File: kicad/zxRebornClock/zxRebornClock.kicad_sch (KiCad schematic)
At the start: 107 parts, among them J1 Jack DC, J2 USB_B_Micro, J3 Conn_01x04, J4 Conn_01x03, J5 Conn_01x03, J6 Conn_01x02, Q1 MMBTA42, Q10 MMBTA42, Q2 MMBTA42, Q3 MMBTA42, Q4 MMBTA42, Q5 MMBTA42, Q6 MMBTA42, Q7 MMBTA42, Q8 MMBTA42, Q9 MMBTA42, SW1 RESET, SW2 D, SW3 HH, SW4 MM, SW5 SS, SW6 F, U1 CH32X035C8T6, U10 TLP627, U2 AMS1117-3.3, U3 12V->200V, U4 USBLC6-4SC6, U5 DS1302, U6 ESP-12F, U7 TLP627, U8 TLP627, U9 TLP627, Y1 32768

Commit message: work in progress
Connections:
- net B_F: now also U1.41 (PA9); no longer U1.24 (PB4)
- net B_HH: now also U1.38 (PC14)
- net B_MM: now also U1.39 (PC15)
- net B_SS: now also U1.40 (PA8); no longer U1.23 (PB3)
- no-connect marks 27 -> 25
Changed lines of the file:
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@@
-	)
-	(no_connect
-		(at 46.99 139.7)
 	)
 	(no_connect
@@
 	)
 	(no_connect
+		(at 57.15 185.42)
+	)
+	(no_connect
 		(at 138.43 232.41)
-	)
-	(no_connect
-		(at 52.07 139.7)
 	)
 	(no_connect
@@
 	)
 	(no_connect
-		(at 49.53 139.7)
-	)
-	(no_connect
 		(at 138.43 224.79)
 	)
@@
 	)
 	(no_connect
-		(at 54.61 139.7)
-	)
-	(no_connect
 		(at 168.91 222.25)
 	)
@@
 	(no_connect
 		(at 20.32 156.21)
+	)
+	(no_connect
+		(at 54.61 185.42)
 	)
 	(no_connect
@@
 	)
 	(label "B_MM"
-		(at 1.905 186.69 0)
+		(at 52.07 139.7 90)
 		(effects
 			(font
@@
 	)
 	(label "B_F"
-		(at 57.15 185.42 270)
-		(effects
-			(font
-				(size 1.27 1.27)
-			)
-			(justify right bottom)
+		(at 46.99 139.7 90)
+		(effects
+			(font
+				(size 1.27 1.27)
+			)
+			(justify left bottom)
 		)
 	)
@@
 	)
 	(label "B_HH"
-		(at 1.905 191.135 0)
+		(at 54.61 139.7 90)
 		(effects
 			(font
@@
 	)
 	(label "B_SS"
-		(at 54.61 185.42 270)
-		(effects
-			(font
-				(size 1.27 1.27)
-			)
-			(justify right bottom)
-		)
-	)
+		(at 49.53 139.7 90)
+		(effects
+			(font
+				(size 1.27 1.27)
+			)
+			(justify left bottom)
+		)
+	)

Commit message: work in progress
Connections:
- net DOWNLOAD: now also U4.3 (I/O2), U4.4 (I/O3); no longer U4.1 (I/O1), U4.6 (I/O4)
- net UDM: now also U4.1 (I/O1), U4.6 (I/O4); no longer U4.3 (I/O2), U4.4 (I/O3)
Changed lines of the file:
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@@
 	)
 	(label "UDP"
-		(at 50.8 204.47 180)
+		(at 50.8 207.01 180)
 		(effects
 			(font
@@
 	)
 	(label "UDM"
-		(at 50.8 207.01 180)
+		(at 50.8 204.47 180)
 		(effects
 			(font
@@
 	)
 	(label "UDM"
-		(at 50.8 209.55 180)
+		(at 50.8 212.09 180)
 		(effects
 			(font
@@
 	)
 	(label "UDP"
-		(at 50.8 212.09 180)
-		(effects
-			(font
+		(at 50.8 209.55 180)
+		(effects
+			(font

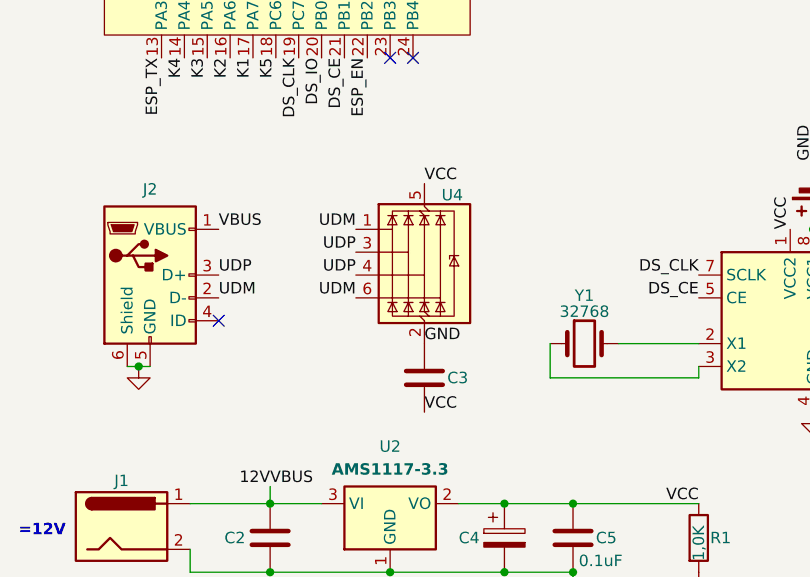
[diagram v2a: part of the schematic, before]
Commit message: fix schema
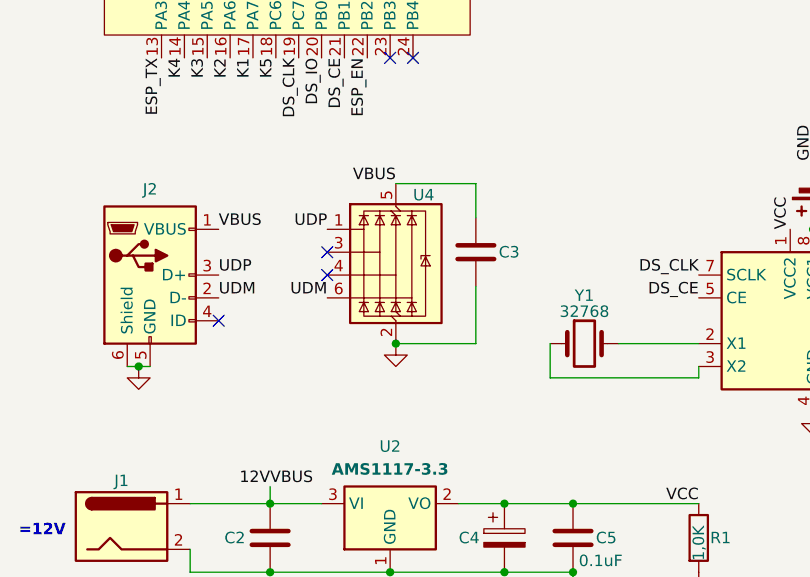
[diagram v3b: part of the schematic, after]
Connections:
- net 12V: now also C3.1, U4.5 (VBUS)
- net DOWNLOAD: now also U4.1 (I/O1); no longer U4.3 (I/O2), U4.4 (I/O3)
- net GND: now also C3.2; no longer C3.1
- net UDM: no longer U4.1 (I/O1)
- net VCC: no longer C3.2, U4.5 (VBUS)
- no-connect marks 25 -> 27
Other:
- moved on the sheet: C3, U4
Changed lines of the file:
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@@
 	)
 	(junction
+		(at 55.245 217.17)
+		(diameter 0)
+		(color 0 0 0 0)
+	)
+	(junction
 		(at 74.93 234.95)
 		(diameter 0)
@@
 	)
 	(no_connect
+		(at 47.625 207.01)
+	)
+	(no_connect
 		(at 138.43 229.87)
 	)
@@
 	)
 	(no_connect
+		(at 47.625 209.55)
+	)
+	(no_connect
 		(at 138.43 219.71)
 	)
@@
 	(wire
 		(pts
+			(xy 55.245 199.39) (xy 64.135 199.39)
+		)
+		(stroke
+			(width 0)
+			(type default)
+		)
+	)
+	(wire
+		(pts
 			(xy 170.18 124.46) (xy 175.26 124.46)
 		)
@@
 	(wire
 		(pts
+			(xy 64.135 210.82) (xy 64.135 217.17)
+		)
+		(stroke
+			(width 0)
+			(type default)
+		)
+	)
+	(wire
+		(pts
 			(xy 184.15 53.975) (xy 184.15 48.895)
 		)
@@
 	(wire
 		(pts
+			(xy 64.135 199.39) (xy 64.135 203.2)
+		)
+		(stroke
+			(width 0)
+			(type default)
+		)
+	)
+	(wire
+		(pts
 			(xy 29.21 137.16) (xy 24.13 137.16)
 		)
@@
 	(wire
 		(pts
+			(xy 64.135 217.17) (xy 55.245 217.17)
+		)
+		(stroke
+			(width 0)
+			(type default)
+		)
+	)
+	(wire
+		(pts
 			(xy 74.93 242.57) (xy 74.93 250.19)
 		)
@@
 		)
 	)
+	(label "VBUS"
+		(at 55.245 199.39 180)
+		(effects
+			(font
+				(size 1.27 1.27)
+			)
+			(justify right bottom)
+		)
+	)
 	(label "0"
 		(at 46.99 109.22 0)
@@
 		)
 	)
+	(label "UDM"
+		(at 47.625 212.09 180)
+		(effects
+			(font
+				(size 1.27 1.27)
+			)
+			(justify right bottom)
+		)
+	)
 	(label "DIO"
 		(at 66.04 153.67 0)
@@
 		)
 	)
-	(label "UDP"
-		(at 50.8 207.01 180)
-		(effects
-			(font
-				(size 1.27 1.27)
-			)
-			(justify right bottom)
-		)
-	)
 	(label "3"
 		(at 21.59 72.39 180)
@@
 		)
 	)
-	(label "UDM"
-		(at 50.8 204.47 180)
-		(effects
-			(font
-				(size 1.27 1.27)
-			)
-			(justify right bottom)
-		)
-	)
 	(label "K4"
 		(at 31.75 185.42 270)
@@
 		)
 	)
-	(label "UDM"
-		(at 50.8 212.09 180)
+	(label "UDP"
+		(at 47.625 204.47 180)
 		(effects
 			(font
@@
 		)
 	)
-	(label "GND"
-		(at 58.42 217.17 0)
-		(effects
-			(font
-				(size 1.27 1.27)
-			)
-			(justify left bottom)
-		)
-	)
 	(label "DOWNLOAD"
 		(at 71.755 156.21 0)
@@
 		)
 	)
-	(label "UDP"
-		(at 50.8 209.55 180)
-		(effects
-			(font
-				(size 1.27 1.27)
-			)
-			(justify right bottom)
-		)
-	)
 	(label "TX"
 		(at 186.69 165.1 180)
@@
 		)
 	)
-	(label "VCC"
-		(at 58.42 199.39 0)
-		(effects
-			(font
-				(size 1.27 1.27)
-			)
-			(justify left bottom)
-		)
-	)
 	(label "B_SS"
 		(at 168.91 187.96 0)
@@
 	)
 	(label "VCC"
-		(at 58.42 224.79 0)
-		(effects
-			(font
-				(size 1.27 1.27)
-			)
-			(justify left bottom)
-		)
-	)
-	(label "VCC"
 		(at 111.125 189.23 180)
 		(effects
@@
 	(symbol
 		(lib_id "Device:C")
-		(at 58.42 220.98 0)
+		(at 64.135 207.01 0)
 		(unit 1)
 		(exclude_from_sim no)
@@
 		(dnp no)
 		(property "Reference" "C3"
-			(at 60.96 220.98 0)
+			(at 66.675 207.01 0)
 			(effects
 				(font
@@
 		)
 		(property "Value" "0,1uF"
-			(at 62.23 222.2499 0)
+			(at 67.945 208.2799 0)
 			(effects
 				(font
@@
 		)
 		(property "Footprint" "Capacitor_SMD:C_0805_2012Metric_Pad1.18x1.45mm_HandSolder"
-			(at 59.3852 224.79 0)
+			(at 65.1002 210.82 0)
 			(effects
 				(font
@@
 		)
 		(property "Datasheet" "~"
-			(at 58.42 220.98 0)
+			(at 64.135 207.01 0)
 			(effects
 				(font
@@
 		)
 		(property "Description" "Unpolarized capacitor"
-			(at 58.42 220.98 0)
+			(at 64.135 207.01 0)
 			(effects
 				(font
@@
 	(symbol
 		(lib_id "Power_Protection:USBLC6-4SC6")
-		(at 58.42 207.01 0)
+		(at 55.245 207.01 0)
 		(unit 1)
 		(exclude_from_sim no)
@@
 		(dnp no)
 		(property "Reference" "U4"
-			(at 60.325 200.66 0)
+			(at 57.15 200.66 0)
 			(effects
 				(font
@@
 		)
 		(property "Value" "USBLC6-4SC6"
-			(at 65.405 209.5499 0)
+			(at 62.23 209.5499 0)
 			(effects
 				(font
@@
 		)
 		(property "Footprint" "Package_TO_SOT_SMD:SOT-23-6"
-			(at 60.96 217.17 0)
+			(at 57.785 217.17 0)
 			(effects
 				(font
@@
 		)
 		(property "Datasheet" "https://www.st.com/resource/en/datasheet/usblc6-4.pdf"
-			(at 60.96 219.71 0)
+			(at 57.785 219.71 0)
 			(effects
 				(font
@@
 		)
 		(property "Description" "Very low capacitance ESD protection diode, 4 data-line, SOT-23-6"
-			(at 58.42 207.01 0)
+			(at 55.245 207.01 0)
 			(effects
 				(font
@@
 					(unit 1)
 				)
+			)
+		)
+	)
+	(symbol
+		(lib_id "power:GND")
+		(at 55.245 217.17 0)
+		(unit 1)
+		(exclude_from_sim no)
+		(in_bom yes)
+		(on_board yes)
+		(dnp no)
+		(fields_autoplaced yes)
+		(property "Reference" "#PWR014"
+			(at 55.245 223.52 0)
+			(effects
+				(font
+					(size 1.27 1.27)
+				)
+				(hide yes)
+			)
+		)
+		(property "Value" "GND"
+			(at 55.245 222.25 0)
+			(effects
+				(font
+					(size 1.27 1.27)
+				)
+				(hide yes)
+			)
+		)
+		(property "Footprint" ""
+			(at 55.245 217.17 0)
+			(effects
+				(font
+					(size 1.27 1.27)
+				)
+				(hide yes)
+			)
+		)
+		(property "Datasheet" ""
+			(at 55.245 217.17 0)
+			(effects
+				(font
+					(size 1.27 1.27)
+				)
+				(hide yes)
+			)
+		)
+		(property "Description" "Power symbol creates a global label with name \"GND\" , ground"
+			(at 55.245 217.17 0)
+			(effects
+				(font
+					(size 1.27 1.27)
+				)
+				(hide yes)
+			)
+		)
+		(pin "1"
+		)
+		(instances
+			(project "zxRebornClock"
+				(path "/1f59fcac-59e1-4c3b-9ba4-e653e2ae108c"
+					(reference "#PWR014")
+					(unit 1)
+				)

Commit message: ibom: work in progress
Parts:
- C1, C3, C6, C7, R35, R36, R37, R38, R39, R40, R41, R42, R43, R44, R45, R46, R47, R48, R51, R52: Note (none) -> 0805
- C2, C5: Link https://aliexpress.ru/item/33007425729.html?sku_id=67085457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 -> (none); Note smd 0805 -> 0805
- C4: Link https://aliexpress.ru/item/4001227639043.html?sku_id=100000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 -> (none); Note (none) -> 10V Polar 8.0х3.5
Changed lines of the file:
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@@
 			)
 		)
+		(property "Note" "0805"
+			(at 64.135 207.01 0)
+			(effects
+				(font
+					(size 1.27 1.27)
+				)
+				(hide yes)
+			)
+		)
 		(pin "1"
 		)
@@
 			)
 		)
+		(property "Note" "0805"
+			(at 187.96 64.135 90)
+			(effects
+				(font
+					(size 1.27 1.27)
+				)
+				(hide yes)
+			)
+		)
 		(pin "2"
 		)
@@
 			)
 		)
+		(property "Note" "0805"
+			(at 163.83 158.75 90)
+			(effects
+				(font
+					(size 1.27 1.27)
+				)
+				(hide yes)
+			)
+		)
 		(pin "1"
 		)
@@
 			)
 		)
-		(property "Link" "https://aliexpress.ru/item/4001227639043.html?sku_id=10000015368849017&spm=a2g2w.stores.seller_list.0.390e2b33TdpRsz"
-			(at 67.31 238.76 0)
-			(effects
-				(font
-					(size 1.27 1.27)
-				)
-				(hide yes)
-			)
-		)
-		(property "Note" ""
+		(property "Note" "10V Polar 8.0х3.5"
 			(at 67.31 238.76 0)
 			(effects
@@
 			)
 		)
+		(property "Note" "0805"
+			(at 187.96 99.695 90)
+			(effects
+				(font
+					(size 1.27 1.27)
+				)
+				(hide yes)
+			)
+		)
 		(pin "2"
 		)
@@
 			)
 		)
+		(property "Note" "0805"
+			(at 187.96 123.19 90)
+			(effects
+				(font
+					(size 1.27 1.27)
+				)
+				(hide yes)
+			)
+		)
 		(pin "2"
 		)
@@
 			)
 		)
+		(property "Note" "0805"
+			(at 187.96 84.455 90)
+			(effects
+				(font
+					(size 1.27 1.27)
+				)
+				(hide yes)
+			)
+		)
 		(pin "2"
 		)
@@
 			)
 		)
+		(property "Note" "0805"
+			(at 187.96 118.11 90)
+			(effects
+				(font
+					(size 1.27 1.27)
+				)
+				(hide yes)
+			)
+		)
 		(pin "2"
 		)
@@
 			)
 		)
+		(property "Note" "0805"
+			(at 187.96 79.375 90)
+			(effects
+				(font
+					(size 1.27 1.27)
+				)
+				(hide yes)
+			)
+		)
 		(pin "2"
 		)
@@
 			)
 		)
+		(property "Note" "0805"
+			(at 153.67 246.38 0)
+			(effects
+				(font
+					(size 1.27 1.27)
+				)
+				(hide yes)
+			)
+		)
 		(pin "1"
 		)
@@
 			)
 		)
+		(property "Note" "0805"
+			(at 187.96 69.215 90)
+			(effects
+				(font
+					(size 1.27 1.27)
+				)
+				(hide yes)
+			)
+		)
 		(pin "2"
 		)
@@
 			)
 		)
+		(property "Note" "0805"
+			(at 187.96 94.615 90)
+			(effects
+				(font
+					(size 1.27 1.27)
+				)
+				(hide yes)
+			)
+		)
 		(pin "2"
 		)
@@
 			)
 		)
+		(property "Note" "0805"
+			(at 187.96 74.295 90)
+			(effects
+				(font
+					(size 1.27 1.27)
+				)
+				(hide yes)
+			)
+		)
 		(pin "2"
 		)
@@
 			)
 		)
+		(property "Note" "0805"
+			(at 187.96 104.775 90)
+			(effects
+				(font
+					(size 1.27 1.27)
+				)
+				(hide yes)
+			)
+		)
 		(pin "2"
 		)
@@
 			)
 		)
+		(property "Note" "0805"
+			(at 187.96 128.27 90)
+			(effects
+				(font
+					(size 1.27 1.27)
+				)
+				(hide yes)
+			)
+		)
 		(pin "2"
 		)
@@
 			)
 		)
-		(property "Link" "https://aliexpress.ru/item/33007425729.html?sku_id=67085457162&spm=a2g2w.stores.seller_list.5.390e2b33TdpRsz"
-			(at 41.275 238.76 0)
-			(effects
-				(font
-					(size 1.27 1.27)
-				)
-				(hide yes)
-			)
-		)
-		(property "Note" "smd 0805"
+		(property "Note" "0805"
 			(at 41.275 238.76 0)
 			(effects
@@
 			)
 		)
+		(property "Note" "0805"
+			(at 187.96 133.35 90)
+			(effects
+				(font
+					(size 1.27 1.27)
+				)
+				(hide yes)
+			)
+		)
 		(pin "2"
 		)
@@
 			)
 		)
+		(property "Note" "0805"
+			(at 187.96 89.535 90)
+			(effects
+				(font
+					(size 1.27 1.27)
+				)
+				(hide yes)
+			)
+		)
 		(pin "2"
 		)
@@
 			)
 		)
+		(property "Note" "0805"
+			(at 187.96 53.975 90)
+			(effects
+				(font
+					(size 1.27 1.27)
+				)
+				(hide yes)
+			)
+		)
 		(pin "2"
 		)
@@
 			)
 		)
+		(property "Note" "0805"
+			(at 27.94 130.81 90)
+			(effects
+				(font
+					(size 1.27 1.27)
+				)
+				(hide yes)
+			)
+		)
 		(pin "1"
 		)
@@
 			)
 		)
-		(property "Link" "https://aliexpress.ru/item/33007425729.html?sku_id=67085457162&spm=a2g2w.stores.seller_list.5.390e2b33TdpRsz"
-			(at 74.93 238.76 0)
-			(effects
-				(font
-					(size 1.27 1.27)
-				)
-				(hide yes)
-			)
-		)
-		(property "Note" "smd 0805"
+		(property "Note" "0805"
 			(at 74.93 238.76 0)
 			(effects
@@
 			)
 		)
+		(property "Note" "0805"
+			(at 187.96 48.895 90)
+			(effects
+				(font
+					(size 1.27 1.27)
+				)
+				(hide yes)
+			)
+		)
 		(pin "2"
 		)
@@
 			(effects
 				(font
+					(size 1.27 1.27)
+				)
+				(hide yes)
+			)
+		)
+		(property "Note" "0805"
+			(at 187.96 59.055 90)
+			(effects
+				(font

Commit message: ibom: work in progress
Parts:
- R16, R17, R18, R19, R2, R20, R29, R3, R30, R31, R32, R33, R4, R5, R6: Note (none) -> 0805
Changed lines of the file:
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@@
 			)
 		)
+		(property "Note" "0805"
+			(at 120.65 104.14 90)
+			(effects
+				(font
+					(size 1.27 1.27)
+				)
+				(hide yes)
+			)
+		)
 		(pin "2"
 		)
@@
 			)
 		)
+		(property "Note" "0805"
+			(at 90.17 85.09 90)
+			(effects
+				(font
+					(size 1.27 1.27)
+				)
+				(hide yes)
+			)
+		)
 		(pin "2"
 		)
@@
 			)
 		)
+		(property "Note" "0805"
+			(at 120.65 123.19 90)
+			(effects
+				(font
+					(size 1.27 1.27)
+				)
+				(hide yes)
+			)
+		)
 		(pin "2"
 		)
@@
 			)
 		)
+		(property "Note" "0805"
+			(at 154.94 187.96 90)
+			(effects
+				(font
+					(size 1.27 1.27)
+				)
+				(hide yes)
+			)
+		)
 		(pin "2"
 		)
@@
 			)
 		)
+		(property "Note" "0805"
+			(at 154.94 194.31 90)
+			(effects
+				(font
+					(size 1.27 1.27)
+				)
+				(hide yes)
+			)
+		)
 		(pin "2"
 		)
@@
 			)
 		)
+		(property "Note" "0805"
+			(at 90.17 123.19 90)
+			(effects
+				(font
+					(size 1.27 1.27)
+				)
+				(hide yes)
+			)
+		)
 		(pin "2"
 		)
@@
 			)
 		)
+		(property "Note" "0805"
+			(at 154.94 168.91 90)
+			(effects
+				(font
+					(size 1.27 1.27)
+				)
+				(hide yes)
+			)
+		)
 		(pin "2"
 		)
@@
 			)
 		)
+		(property "Note" "0805"
+			(at 154.94 175.26 90)
+			(effects
+				(font
+					(size 1.27 1.27)
+				)
+				(hide yes)
+			)
+		)
 		(pin "2"
 		)
@@
 			)
 		)
+		(property "Note" "0805"
+			(at 90.17 66.04 90)
+			(effects
+				(font
+					(size 1.27 1.27)
+				)
+				(hide yes)
+			)
+		)
 		(pin "2"
 		)
@@
 			)
 		)
+		(property "Note" "0805"
+			(at 154.94 181.61 90)
+			(effects
+				(font
+					(size 1.27 1.27)
+				)
+				(hide yes)
+			)
+		)
 		(pin "2"
 		)
@@
 			)
 		)
+		(property "Note" "0805"
+			(at 120.65 85.09 90)
+			(effects
+				(font
+					(size 1.27 1.27)
+				)
+				(hide yes)
+			)
+		)
 		(pin "2"
 		)
@@
 			)
 		)
+		(property "Note" "0805"
+			(at 120.65 66.04 90)
+			(effects
+				(font
+					(size 1.27 1.27)
+				)
+				(hide yes)
+			)
+		)
 		(pin "2"
 		)
@@
 			)
 		)
+		(property "Note" "0805"
+			(at 90.17 142.24 90)
+			(effects
+				(font
+					(size 1.27 1.27)
+				)
+				(hide yes)
+			)
+		)
 		(pin "2"
 		)
@@
 			)
 		)
+		(property "Note" "0805"
+			(at 120.65 142.24 90)
+			(effects
+				(font
+					(size 1.27 1.27)
+				)
+				(hide yes)
+			)
+		)
 		(pin "2"
 		)
@@
 			(effects
 				(font
+					(size 1.27 1.27)
+				)
+				(hide yes)
+			)
+		)
+		(property "Note" "0805"
+			(at 90.17 104.14 90)
+			(effects
+				(font

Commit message: ibom: work in progress
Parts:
- R10, R11, R21, R22, R23, R24, R25, R7, R8, R9: Note (none) -> 0805
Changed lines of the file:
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@@
 			)
 		)
+		(property "Note" "0805"
+			(at 124.46 127 90)
+			(effects
+				(font
+					(size 1.27 1.27)
+				)
+				(hide yes)
+			)
+		)
 		(pin "2"
 		)
@@
 			)
 		)
+		(property "Note" "0805"
+			(at 124.46 107.95 90)
+			(effects
+				(font
+					(size 1.27 1.27)
+				)
+				(hide yes)
+			)
+		)
 		(pin "2"
 		)
@@
 			)
 		)
+		(property "Note" "0805"
+			(at 93.98 127 90)
+			(effects
+				(font
+					(size 1.27 1.27)
+				)
+				(hide yes)
+			)
+		)
 		(pin "2"
 		)
@@
 			)
 		)
+		(property "Note" "0805"
+			(at 124.46 69.85 90)
+			(effects
+				(font
+					(size 1.27 1.27)
+				)
+				(hide yes)
+			)
+		)
 		(pin "2"
 		)
@@
 			)
 		)
+		(property "Note" "0805"
+			(at 93.98 69.85 90)
+			(effects
+				(font
+					(size 1.27 1.27)
+				)
+				(hide yes)
+			)
+		)
 		(pin "2"
 		)
@@
 			)
 		)
+		(property "Note" "0805"
+			(at 93.98 107.95 90)
+			(effects
+				(font
+					(size 1.27 1.27)
+				)
+				(hide yes)
+			)
+		)
 		(pin "2"
 		)
@@
 			)
 		)
+		(property "Note" "0805"
+			(at 124.46 88.9 90)
+			(effects
+				(font
+					(size 1.27 1.27)
+				)
+				(hide yes)
+			)
+		)
 		(pin "2"
 		)
@@
 			)
 		)
+		(property "Note" "0805"
+			(at 124.46 146.05 90)
+			(effects
+				(font
+					(size 1.27 1.27)
+				)
+				(hide yes)
+			)
+		)
 		(pin "2"
 		)
@@
 			)
 		)
+		(property "Note" "0805"
+			(at 93.98 146.05 90)
+			(effects
+				(font
+					(size 1.27 1.27)
+				)
+				(hide yes)
+			)
+		)
 		(pin "2"
 		)
@@
 			(effects
 				(font
+					(size 1.27 1.27)
+				)
+				(hide yes)
+			)
+		)
+		(property "Note" "0805"
+			(at 93.98 88.9 90)
+			(effects
+				(font

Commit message: ibom: work in progress
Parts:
- R1, R12, R13, R14, R15, R26, R27, R34, R49, R50: Note (none) -> 0805
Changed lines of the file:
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@@
 			)
 		)
+		(property "Note" "0805"
+			(at 134.62 214.63 90)
+			(effects
+				(font
+					(size 1.27 1.27)
+				)
+				(hide yes)
+			)
+		)
 		(pin "2"
 		)
@@
 			)
 		)
+		(property "Note" "0805"
+			(at 172.72 232.41 90)
+			(effects
+				(font
+					(size 1.27 1.27)
+				)
+				(hide yes)
+			)
+		)
 		(pin "2"
 		)
@@
 			)
 		)
+		(property "Note" "0805"
+			(at 188.595 209.55 90)
+			(effects
+				(font
+					(size 1.27 1.27)
+				)
+				(hide yes)
+			)
+		)
 		(pin "2"
 		)
@@
 			)
 		)
+		(property "Note" "0805"
+			(at 134.62 209.55 90)
+			(effects
+				(font
+					(size 1.27 1.27)
+				)
+				(hide yes)
+			)
+		)
 		(pin "2"
 		)
@@
 			)
 		)
+		(property "Note" "0805"
+			(at 114.935 182.88 90)
+			(effects
+				(font
+					(size 1.27 1.27)
+				)
+				(hide yes)
+			)
+		)
 		(pin "2"
 		)
@@
 			)
 		)
+		(property "Note" "0805"
+			(at 88.9 238.76 0)
+			(effects
+				(font
+					(size 1.27 1.27)
+				)
+				(hide yes)
+			)
+		)
 		(pin "1"
 		)
@@
 			)
 		)
+		(property "Note" "0805"
+			(at 188.595 214.63 90)
+			(effects
+				(font
+					(size 1.27 1.27)
+				)
+				(hide yes)
+			)
+		)
 		(pin "2"
 		)
@@
 			)
 		)
+		(property "Note" "0805"
+			(at 114.935 189.23 90)
+			(effects
+				(font
+					(size 1.27 1.27)
+				)
+				(hide yes)
+			)
+		)
 		(pin "2"
 		)
@@
 			)
 		)
+		(property "Note" "0805"
+			(at 114.935 194.945 90)
+			(effects
+				(font
+					(size 1.27 1.27)
+				)
+				(hide yes)
+			)
+		)
 		(pin "2"
 		)
@@
 			(effects
 				(font
+					(size 1.27 1.27)
+				)
+				(hide yes)
+			)
+		)
+		(property "Note" "0805"
+			(at 114.935 176.53 90)
+			(effects
+				(font

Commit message: ibom: work in progress
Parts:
- D1, D2, D3, D4, D5: Note (none) -> led 0805
- R28: Note (none) -> 0805
- U10, U7, U8, U9: Note (none) -> или KP40101D
- U3: Note (none) -> https://github.com/popovb/NixiePowerSupply
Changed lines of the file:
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@@
 			)
 		)
+		(property "Note" "led 0805"
+			(at 122.555 194.945 0)
+			(effects
+				(font
+					(size 1.27 1.27)
+				)
+				(hide yes)
+			)
+		)
 		(pin "1"
 		)
@@
 			)
 		)
+		(property "Note" "led 0805"
+			(at 88.9 246.38 90)
+			(effects
+				(font
+					(size 1.27 1.27)
+				)
+				(hide yes)
+			)
+		)
 		(pin "1"
 		)
@@
 			)
 		)
+		(property "Note" "led 0805"
+			(at 122.555 176.53 0)
+			(effects
+				(font
+					(size 1.27 1.27)
+				)
+				(hide yes)
+			)
+		)
 		(pin "1"
 		)
@@
 			)
 		)
+		(property "Note" "https://github.com/popovb/NixiePowerSupply"
+			(at 54.61 255.905 0)
+			(effects
+				(font
+					(size 1.27 1.27)
+				)
+				(hide yes)
+			)
+		)
 		(instances
 			(project ""
@@
 			)
 		)
+		(property "Note" "led 0805"
+			(at 122.555 182.88 0)
+			(effects
+				(font
+					(size 1.27 1.27)
+				)
+				(hide yes)
+			)
+		)
 		(pin "1"
 		)
@@
 			)
 		)
+		(property "Note" "или KP40101D"
+			(at 162.56 88.9 0)
+			(effects
+				(font
+					(size 1.27 1.27)
+				)
+				(hide yes)
+			)
+		)
 		(pin "3"
 		)
@@
 			)
 		)
+		(property "Note" "или KP40101D"
+			(at 162.56 114.3 0)
+			(effects
+				(font
+					(size 1.27 1.27)
+				)
+				(hide yes)
+			)
+		)
 		(pin "3"
 		)
@@
 			)
 		)
+		(property "Note" "led 0805"
+			(at 122.555 189.23 0)
+			(effects
+				(font
+					(size 1.27 1.27)
+				)
+				(hide yes)
+			)
+		)
 		(pin "1"
 		)
@@
 			)
 		)
+		(property "Note" "или KP40101D"
+			(at 162.56 127 0)
+			(effects
+				(font
+					(size 1.27 1.27)
+				)
+				(hide yes)
+			)
+		)
 		(pin "3"
 		)
@@
 			)
 		)
+		(property "Note" "или KP40101D"
+			(at 162.56 101.6 0)
+			(effects
+				(font
+					(size 1.27 1.27)
+				)
+				(hide yes)
+			)
+		)
 		(pin "3"
 		)
@@
 			(effects
 				(font
+					(size 1.27 1.27)
+				)
+				(hide yes)
+			)
+		)
+		(property "Note" "0805"
+			(at 154.94 137.16 90)
+			(effects
+				(font
